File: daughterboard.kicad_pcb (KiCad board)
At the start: 4 copper layers, 70 x 90 mm, 69 parts, among them J1 USB_OTG, J10 J, J11 J, J12 J, J13 J, J14 J, J15 J, J16 J, J17 J, J18 J, J19 J, J2 MotorA, J20 J, J21 J, J22 J, J23 J, J24 J, J25 J, J26 J, J27 J, J28 J, J29 J, J3 MotorB, J30 J, J31 J, J32 J, J33 QTR-8A, J34 J, J35 J, J36 J, J37 J, J4 BARREL_JACK, J5 Debug, J6 J, J7 J, J8 J, J9 J, SW1 Reset, U1 LD1117S33CTR, U2 TB6612FNG, U3 EFM32G230F128, Y1 Crystal

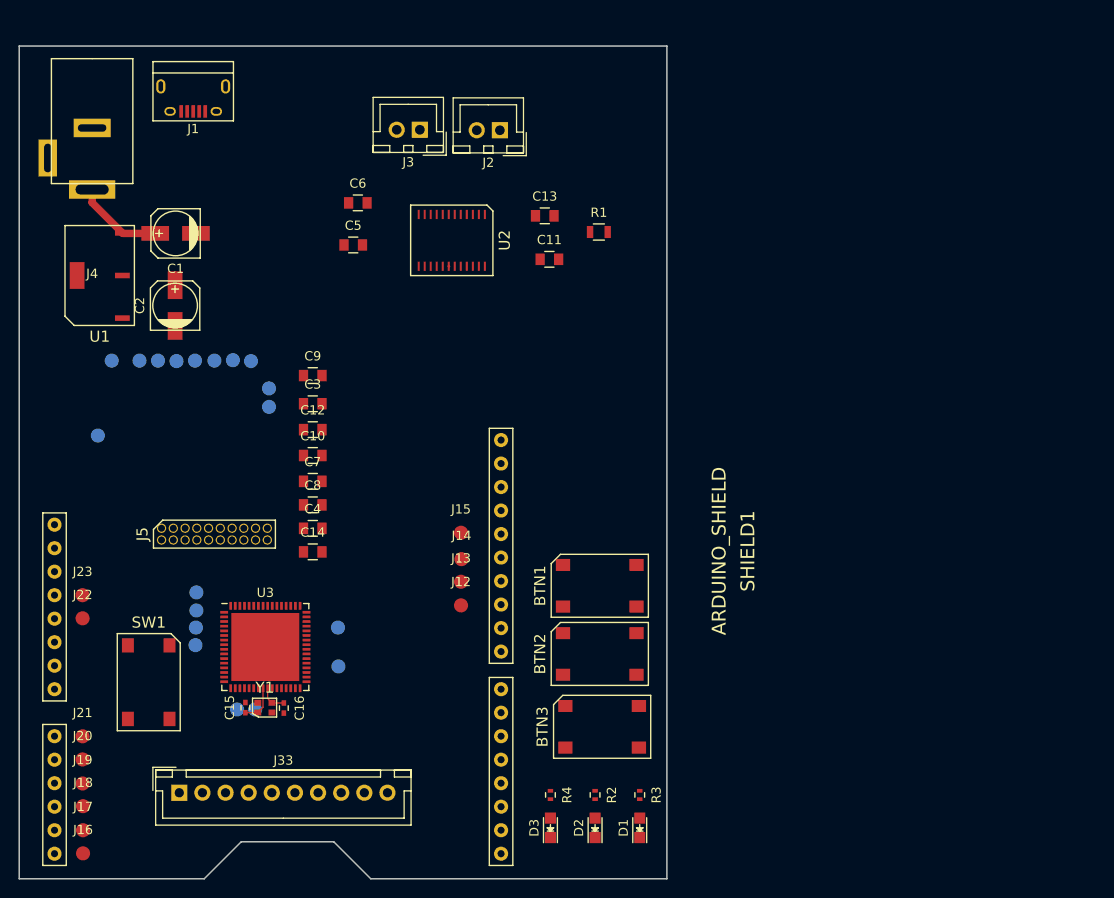
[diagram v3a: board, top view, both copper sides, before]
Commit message: Use new, smaller components
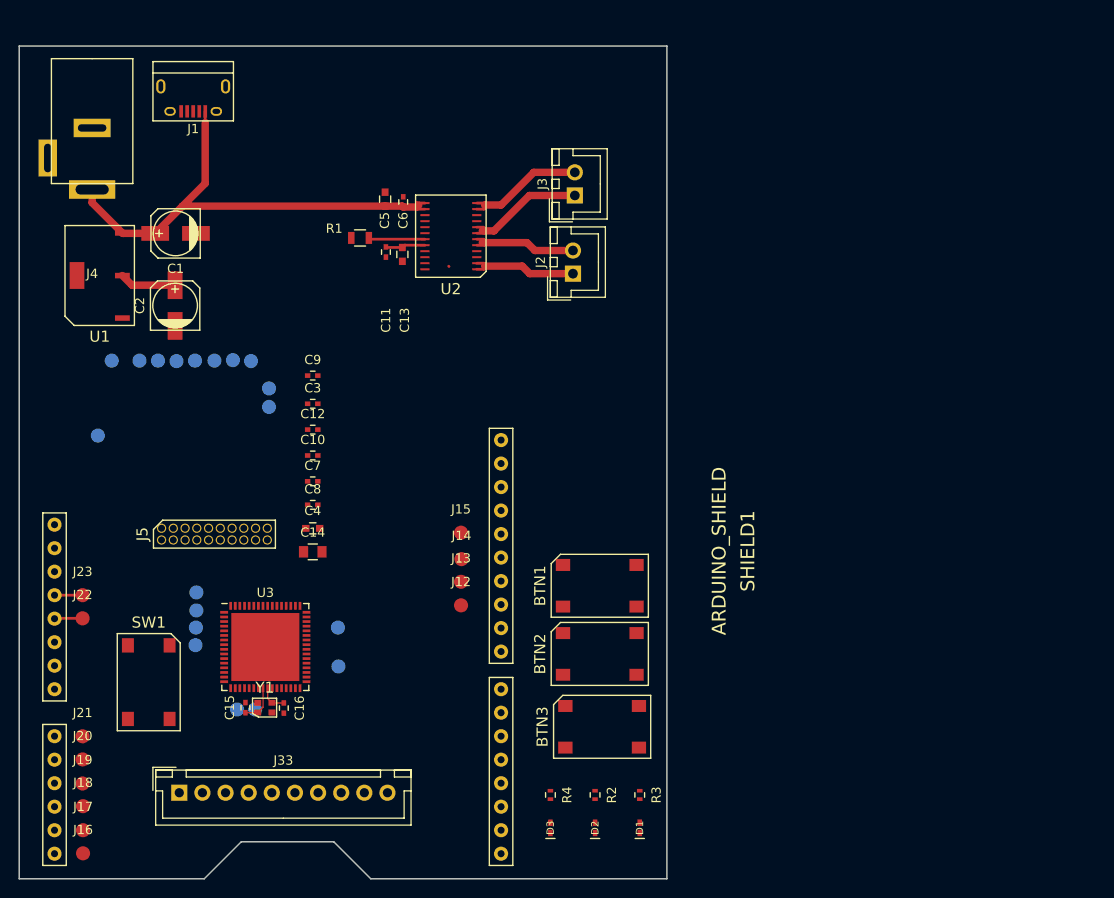
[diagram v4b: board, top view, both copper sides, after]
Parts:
- C10, C11, C12, C3, C6, C7, C8, C9: footprint Capacitors_SMD:C_0805 -> Capacitors_SMD:C_0402
- C13, C4, C5: footprint Capacitors_SMD:C_0805 -> Capacitors_SMD:C_0603
- D1, D2, D3: footprint LEDs:LED_0805 -> lib_fp:LED-0402
- moved R1 25.8 mm to (100.8, 78.7), turned to 180 degrees
- moved J3 18.2 mm to (124.0, 74.2), turned to 90 degrees
- moved C11 17.7 mm to (103.6, 80.3), turned to 270 degrees
- moved J2 17.4 mm to (123.8, 82.6), turned to 90 degrees
- moved C13 15.9 mm to (105.4, 80.5), turned to 270 degrees
- moved C5 6.03 mm to (103.5, 74.5), turned to 90 degrees
- moved C6 4.90 mm to (105.5, 74.8), turned to 90 degrees
- moved U2 0.46 mm to (110.7, 78.5), turned to 90 degrees
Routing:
- net +5V: track 9.62 -> 53.3 mm
- net /TB6612/MotorB2: track 0.00 -> 13.8 mm
- net /TB6612/MotorB1: track 0.00 -> 13.6 mm
- net /TB6612/MotorA2: track 0.00 -> 12.4 mm
- net /TB6612/MotorA1: track 0.00 -> 12.2 mm
- net +3V3: track 0.00 -> 10.5 mm
- net /TB6612/STBY: track 0.00 -> 6.12 mm
- net Net-(J22-Pad1): track 0.00 -> 3.05 mm
- net Net-(J23-Pad1): track 0.00 -> 3.03 mm

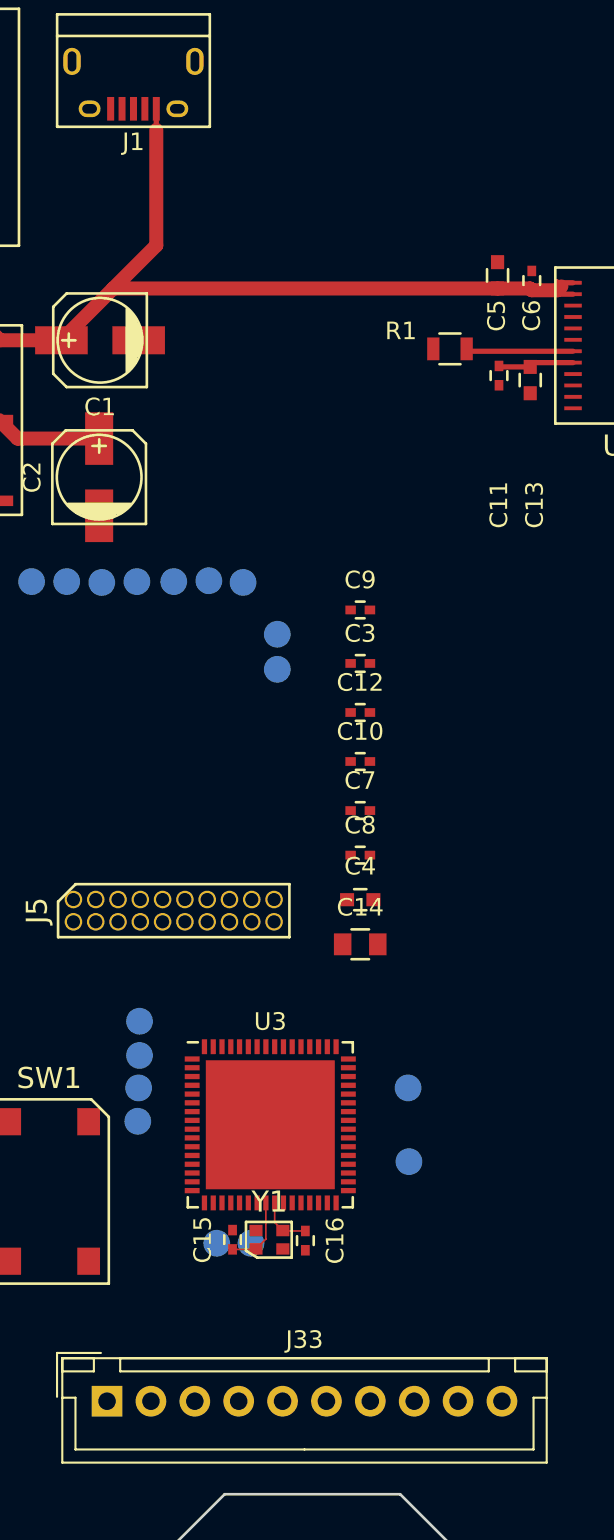
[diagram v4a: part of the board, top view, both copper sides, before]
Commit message: Route connection QTR-8A
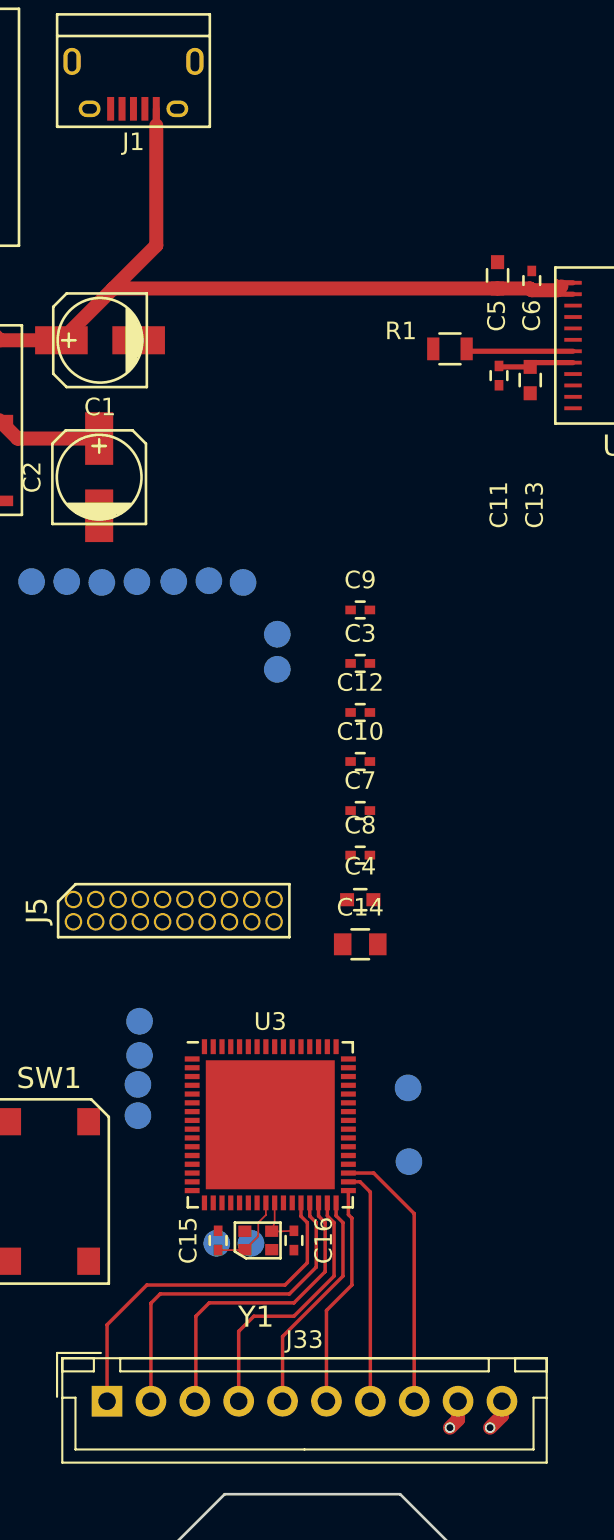
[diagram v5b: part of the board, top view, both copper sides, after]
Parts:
- moved J34 2.10 mm to (83.1, 120.7)
- moved J35 1.58 mm to (83.1, 122.4)
- moved C15 0.82 mm to (87.6, 129.5)
- moved C16 0.65 mm to (91.9, 129.5)
- moved Y1 0.64 mm to (89.9, 129.5)
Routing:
- net /EFM32/ADC0_CH0: track 0.00 -> 20.8 mm
- net /EFM32/ADC0_CH1: track 0.00 -> 19.7 mm
- net /EFM32/ADC0_CH2: track 0.00 -> 17.4 mm
- net /EFM32/ADC0_CH7: track 0.00 -> 15.4 mm
- net /EFM32/ADC0_CH3: track 0.00 -> 15.0 mm
- net /EFM32/ADC0_CH6: track 0.00 -> 13.4 mm
- net /EFM32/ADC0_CH4: track 0.00 -> 12.9 mm
- net /EFM32/ADC0_CH5: track 0.00 -> 12.7 mm
- net +3V3: track 10.5 -> 13.0 mm, vias 0 -> 1
- net GND: track 0.00 -> 1.79 mm, vias 0 -> 1

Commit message: Route TB6612
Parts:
- removed J36, J37: J, Measurement_Points:Measurement_Point_Round-SMD-Pad_Small
- J22, J23: moved to B.Cu
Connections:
- SHIELD1 pad 9: /EFM32/PC7 -> Net-(SHIELD1-Pad9)
- U3 pad 17: /EFM32/PWMB -> /EFM32/PA8
- U3 pad 38: /EFM32/PC7 -> /EFM32/AIN2
- U3 pad 41: /EFM32/AIN1 -> /EFM32/PWMB
- U3 pad 42: /EFM32/AIN2 -> /EFM32/AIN1
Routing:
- net /EFM32/PWMB: track 0.00 -> 58.7 mm, vias 0 -> 2
- net GND: track 1.79 -> 56.2 mm, vias 1 -> 9
- net /EFM32/BIN1: track 0.00 -> 53.6 mm, vias 0 -> 2
- net /EFM32/AIN2: track 0.00 -> 53.3 mm, vias 0 -> 2
- net /EFM32/BIN2: track 0.00 -> 53.1 mm
- net /EFM32/AIN1: track 0.00 -> 52.2 mm, vias 0 -> 2
- net /EFM32/PWMA: track 0.00 -> 46.8 mm
- net +5V: track 53.3 -> 61.1 mm, vias 0 -> 2
- net +3V3: track 13.0 -> 20.2 mm, vias 1 -> 3
- net Net-(J23-Pad1): track 3.03 -> 0.00 mm
- net Net-(J22-Pad1): track 3.05 -> 0.05 mm
- net (no net): track 0.04 -> 2.32 mm

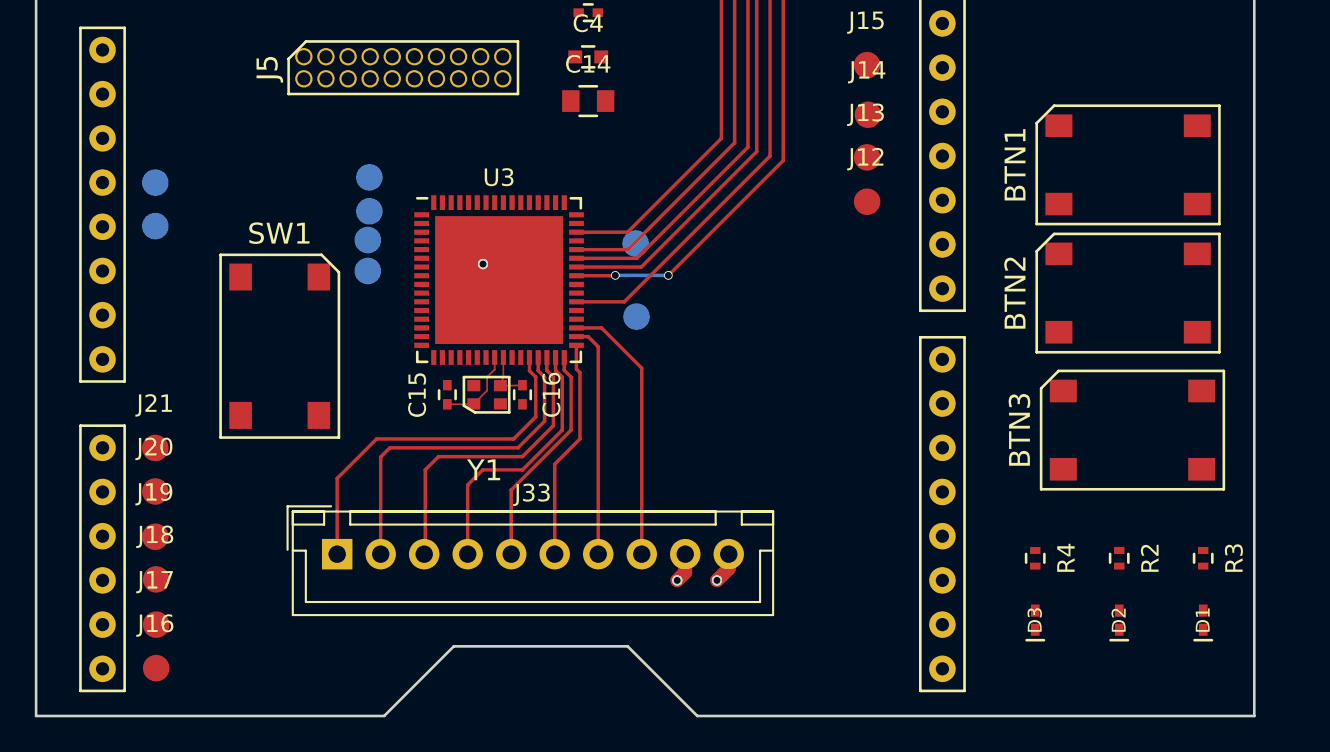
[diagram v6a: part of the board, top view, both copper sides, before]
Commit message: Create and use footprint for new, smaller switches
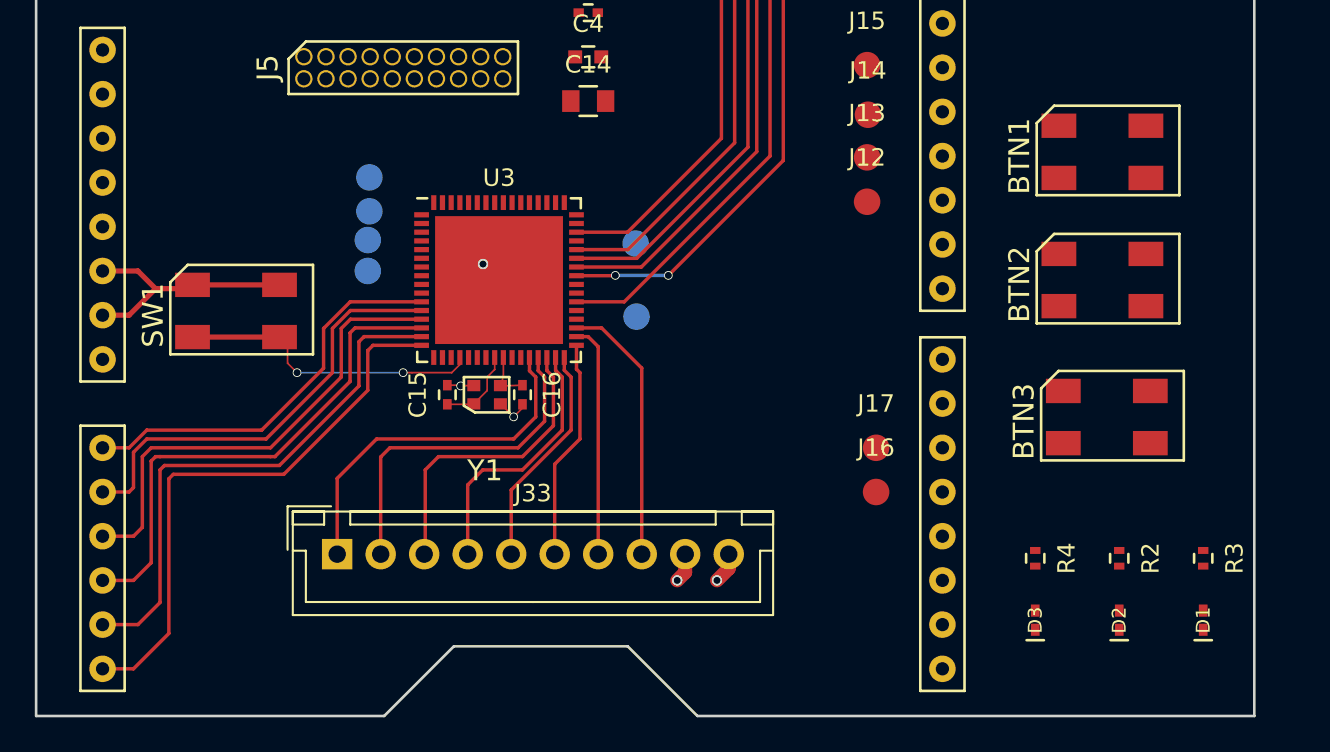
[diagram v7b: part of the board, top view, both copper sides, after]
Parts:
- removed J18, J19, J20, J21, J22, J23: J, Measurement_Points:Measurement_Point_Round-SMD-Pad_Small
- BTN1, BTN2, BTN3, SW1: footprint footprints:SW-4 -> lib_fp:Small_switch
- moved J17 42.6 mm to (112.3, 132.6)
- moved J16 42.6 mm to (112.3, 135.1)
- moved SW1 1.64 mm to (77.0, 125.5), turned to 0 degrees
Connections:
- BTN1 pad 1: Net-(BTN1-Pad1) -> +3V3
- BTN1 pad 2: /EFM32/PA15 -> +3V3
- BTN1 pad 3: +3V3 -> /EFM32/PA15
- BTN1 pad 4: Net-(BTN1-Pad4) -> /EFM32/PA15
- BTN2 pad 1: Net-(BTN2-Pad1) -> +3V3
- BTN2 pad 2: /EFM32/PA10 -> +3V3
- BTN2 pad 3: +3V3 -> /EFM32/PA10
- BTN2 pad 4: Net-(BTN2-Pad4) -> /EFM32/PA10
- BTN3 pad 1: Net-(BTN3-Pad1) -> +3V3
- BTN3 pad 2: /EFM32/PA9 -> +3V3
- BTN3 pad 3: +3V3 -> /EFM32/PA9
- BTN3 pad 4: Net-(BTN3-Pad4) -> /EFM32/PA9
- J10 pad 1: /EFM32/PB7 -> Net-(J10-Pad1)
- J11 pad 1: /EFM32/PB8 -> Net-(J11-Pad1)
- J16 pad 1: /AD5 -> Net-(J16-Pad1)
- J17 pad 1: /AD4 -> Net-(J17-Pad1)
- SHIELD1 pad 2: /EFM32/PC5 -> Net-(J10-Pad1)
- SHIELD1 pad 3: /EFM32/PC4 -> Net-(J11-Pad1)
- SHIELD1 pad 4: /EFM32/PC3 -> Net-(J16-Pad1)
- SHIELD1 pad 5: /EFM32/PC2 -> Net-(J17-Pad1)
- SHIELD1 pad A0: /AD0 -> /EFM32/PC2
- SHIELD1 pad A1: /AD1 -> /EFM32/PC3
- SHIELD1 pad A2: /AD2 -> /EFM32/PC4
- SHIELD1 pad A3: /AD3 -> /EFM32/PC5
- SHIELD1 pad A4: /AD4 -> /EFM32/PB7
- SHIELD1 pad A5: /AD5 -> /EFM32/PB8
- SW1 pad 1: Net-(SW1-Pad1) -> GND
- SW1 pad 2: /EFM32/RESETn -> GND
- SW1 pad 3: GND -> /EFM32/RESETn
- SW1 pad 4: Net-(SW1-Pad4) -> /EFM32/RESETn
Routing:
- net /EFM32/PB8: track 0.00 -> 32.6 mm
- net /EFM32/PB7: track 0.00 -> 31.1 mm
- net /EFM32/PC5: track 0.00 -> 29.4 mm
- net /EFM32/PC4: track 0.00 -> 27.5 mm
- net /EFM32/PC3: track 0.00 -> 25.3 mm
- net /EFM32/PC2: track 0.00 -> 23.1 mm
- net GND: track 56.2 -> 74.1 mm, vias 9 -> 11
- net /EFM32/RESETn: track 0.00 -> 17.0 mm, vias 0 -> 2
